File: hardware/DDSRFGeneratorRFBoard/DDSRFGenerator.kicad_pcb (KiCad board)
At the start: 2 copper layers, 72 parts, among them J1 Conn_Coaxial, K1 FINDER-44.52, K2 FINDER-44.52, K3 FINDER-44.52, Q1 Q_NPN_BEC, Q2 Q_NPN_BEC, Q3 Q_NPN_BEC, U1 TC1107-3.3VOA, U2 L7805, U3 L7805, U4 AD9832

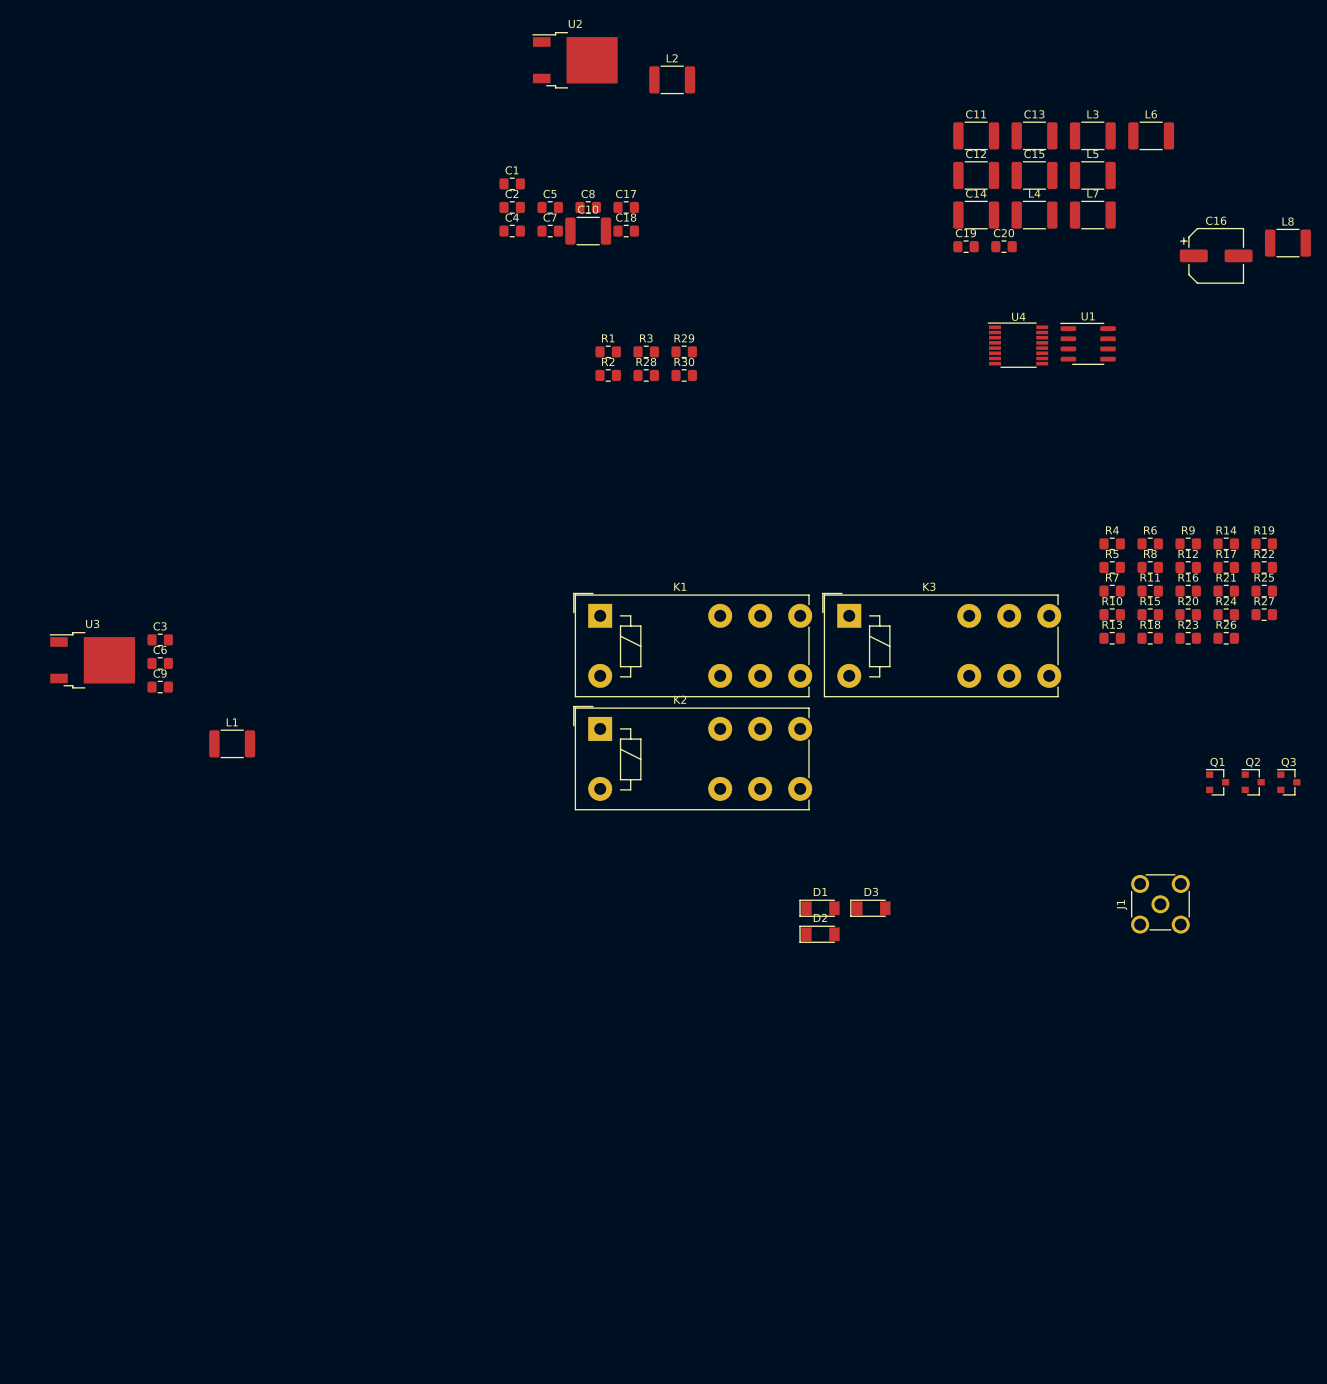
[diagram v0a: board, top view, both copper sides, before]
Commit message: draft of correct relay connections
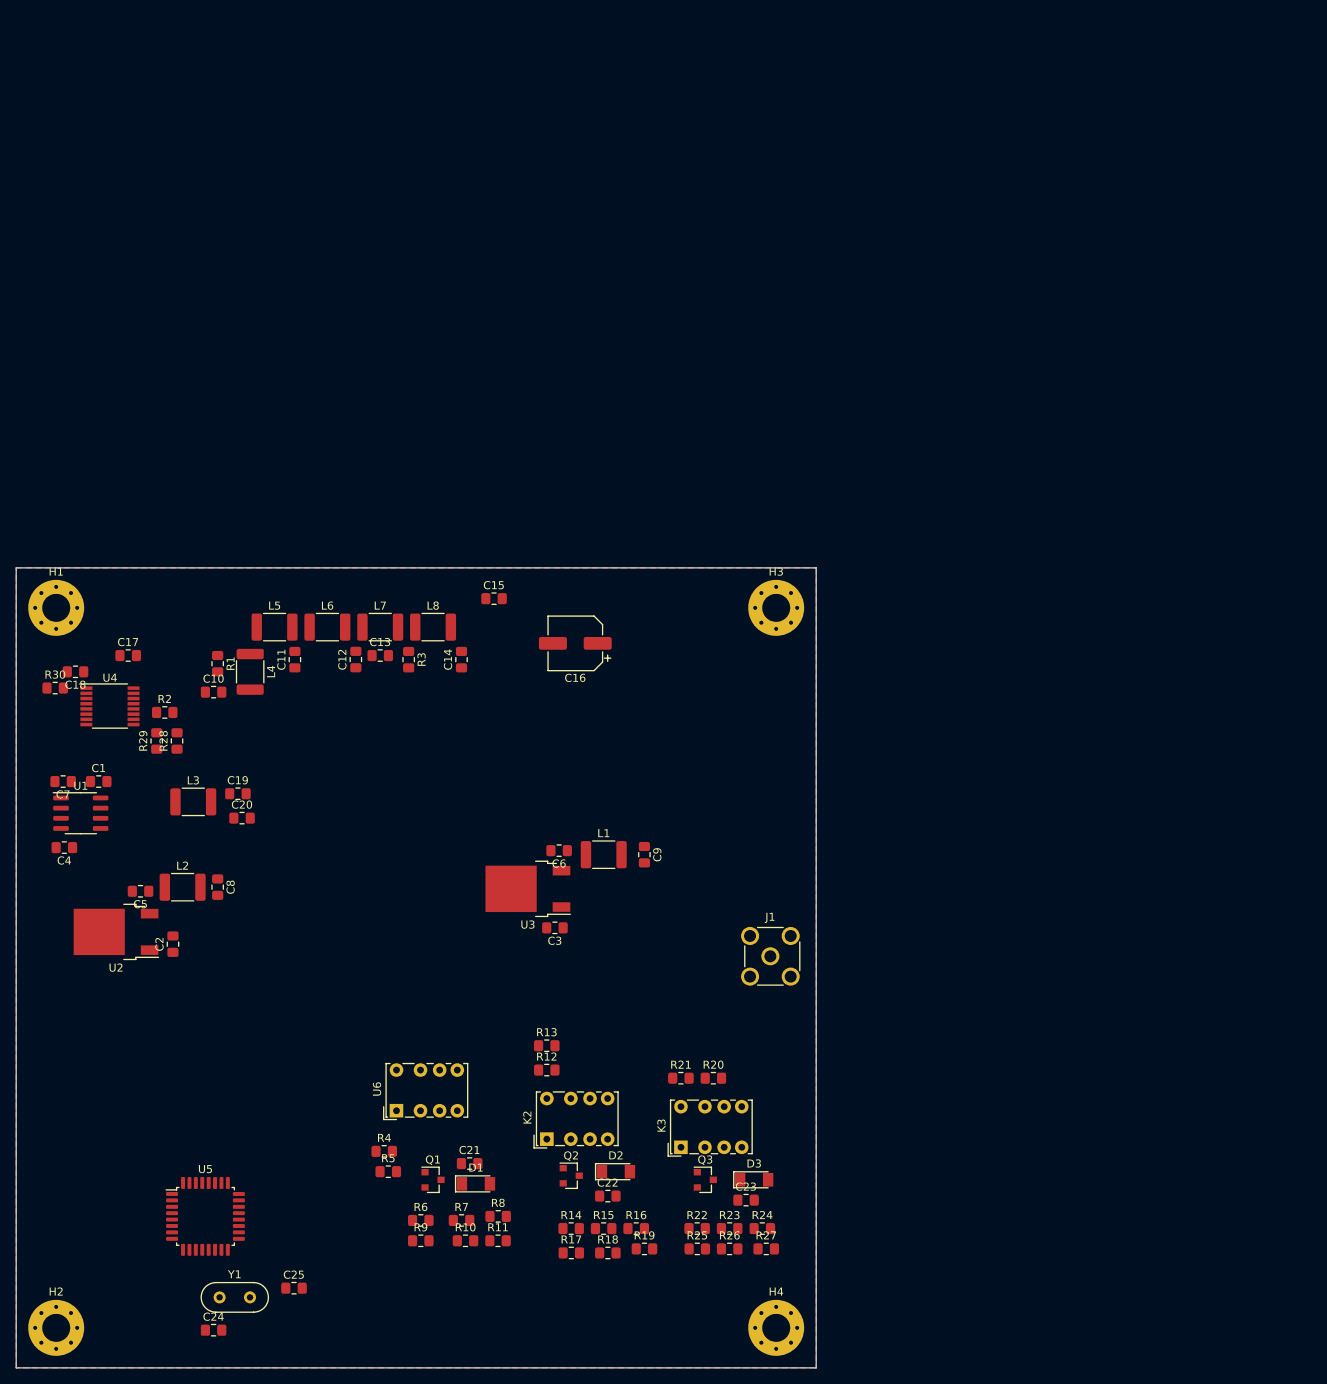
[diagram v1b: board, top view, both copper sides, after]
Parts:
- removed K1: FINDER-44.52, Relay_THT:Relay_DPDT_Finder_40.52
- added C21: 1n, Capacitor_SMD:C_0805_2012Metric_Pad1.15x1.40mm_HandSolder, F.Cu at (106.7, 124.5)
- added C22: 1n, Capacitor_SMD:C_0805_2012Metric_Pad1.15x1.40mm_HandSolder, F.Cu at (124.0, 128.5)
- added C23: 1n, Capacitor_SMD:C_0805_2012Metric_Pad1.15x1.40mm_HandSolder, F.Cu at (141.2, 129.0)
- added C24: 20p, Capacitor_SMD:C_0805_2012Metric_Pad1.15x1.40mm_HandSolder, F.Cu at (74.7, 145.3)
- added C25: 20p, Capacitor_SMD:C_0805_2012Metric_Pad1.15x1.40mm_HandSolder, F.Cu at (84.7, 140.0)
- added H1: MountingHole_Pad, MountingHole:MountingHole_3.5mm_Pad_Via, F.Cu at (55.0, 55.0)
- added H2: MountingHole_Pad, MountingHole:MountingHole_3.5mm_Pad_Via, F.Cu at (55.0, 145.0)
- added H3: MountingHole_Pad, MountingHole:MountingHole_3.5mm_Pad_Via, F.Cu at (145.0, 55.0)
- added H4: MountingHole_Pad, MountingHole:MountingHole_3.5mm_Pad_Via, F.Cu at (145.0, 145.0)
- added U5: STM32F030K6Tx, Package_QFP:LQFP-32_7x7mm_P0.8mm, F.Cu at (73.7, 131.1)
- added U6: RSM850B-6112-85-1005, Relay_THT:Relay_DPDT_Omron_G6K-2P-Y, F.Cu at (97.5, 117.9)
- added Y1: Crystal, Crystal:Crystal_HC52-6mm_Vertical, F.Cu at (75.4, 141.2)
- C10, C11, C12, C13, C14, C15: footprint Inductor_SMD:L_1812_4532Metric_Pad1.30x3.40mm_HandSolder -> Capacitor_SMD:C_0805_2012Metric_Pad1.15x1.40mm_HandSolder
- K2, K3: footprint Relay_THT:Relay_DPDT_Finder_40.52 -> Relay_THT:Relay_DPDT_Omron_G6K-2P-Y
- moved L3 139.9 mm to (72.1, 79.2)
- moved U1 138.9 mm to (58.1, 80.7)
- moved R9 129.6 mm to (100.6, 134.1)
- moved R6 124.4 mm to (100.6, 131.6)
- moved U2 123.2 mm to (62.5, 95.5), turned to 180 degrees
- moved U4 122.2 mm to (61.7, 67.3)
- moved L6 119.9 mm to (88.9, 57.4)
- moved C20 119.1 mm to (78.2, 81.3)
- moved R4 118.5 mm to (96.0, 122.9)
- moved R17 118.5 mm to (119.4, 135.6)
- moved R14 118.4 mm to (119.4, 132.6)
- moved L2 118.0 mm to (70.8, 89.9)
- moved R5 117.9 mm to (96.5, 125.5)
- moved R19 117.3 mm to (128.5, 135.1)
- moved L8 117.1 mm to (102.1, 57.4)
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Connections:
- net Net-(R29-Pad2) renamed FSELECT
- J1 pad 1: Net-(J1-Pad1) -> (no net)
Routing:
- added copper zone on F.Cu, net GND
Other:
- board outline added: 100 x 100 mm

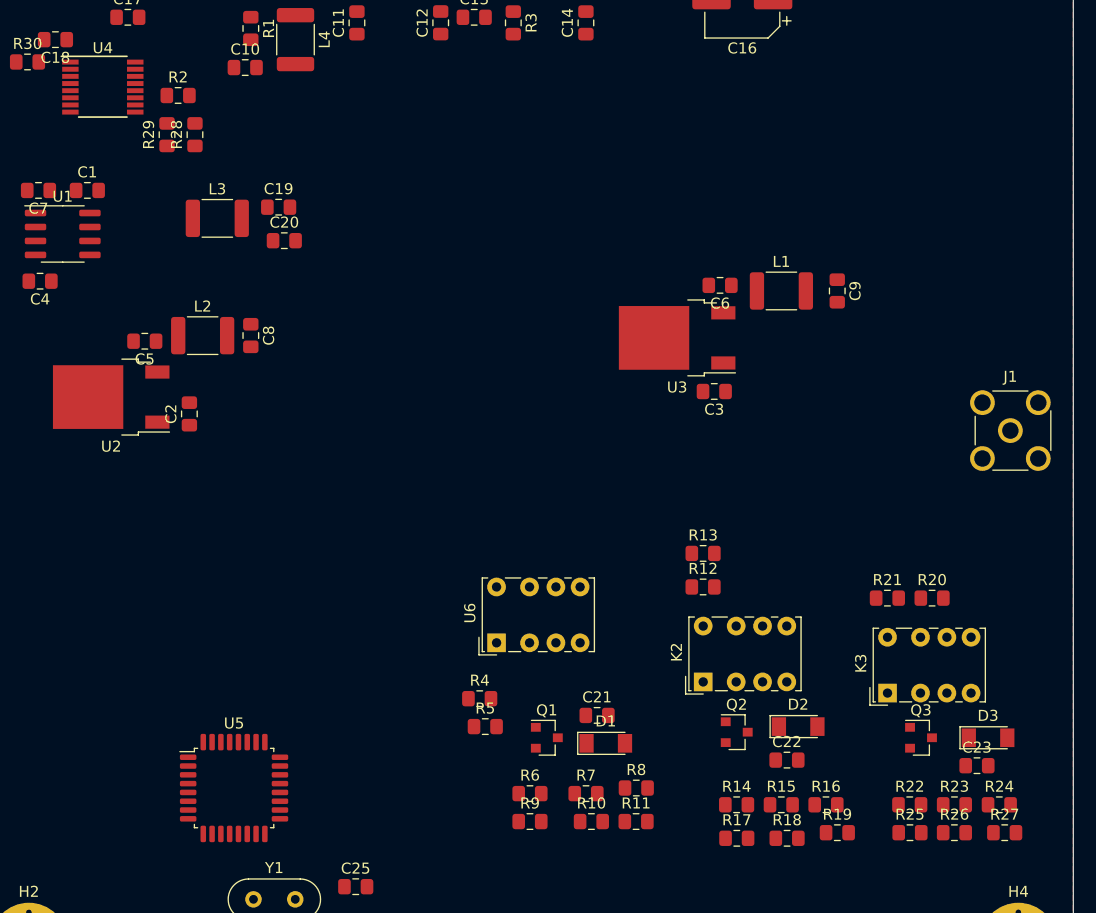
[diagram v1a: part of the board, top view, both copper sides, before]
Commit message: rougly placed submodules on pcb
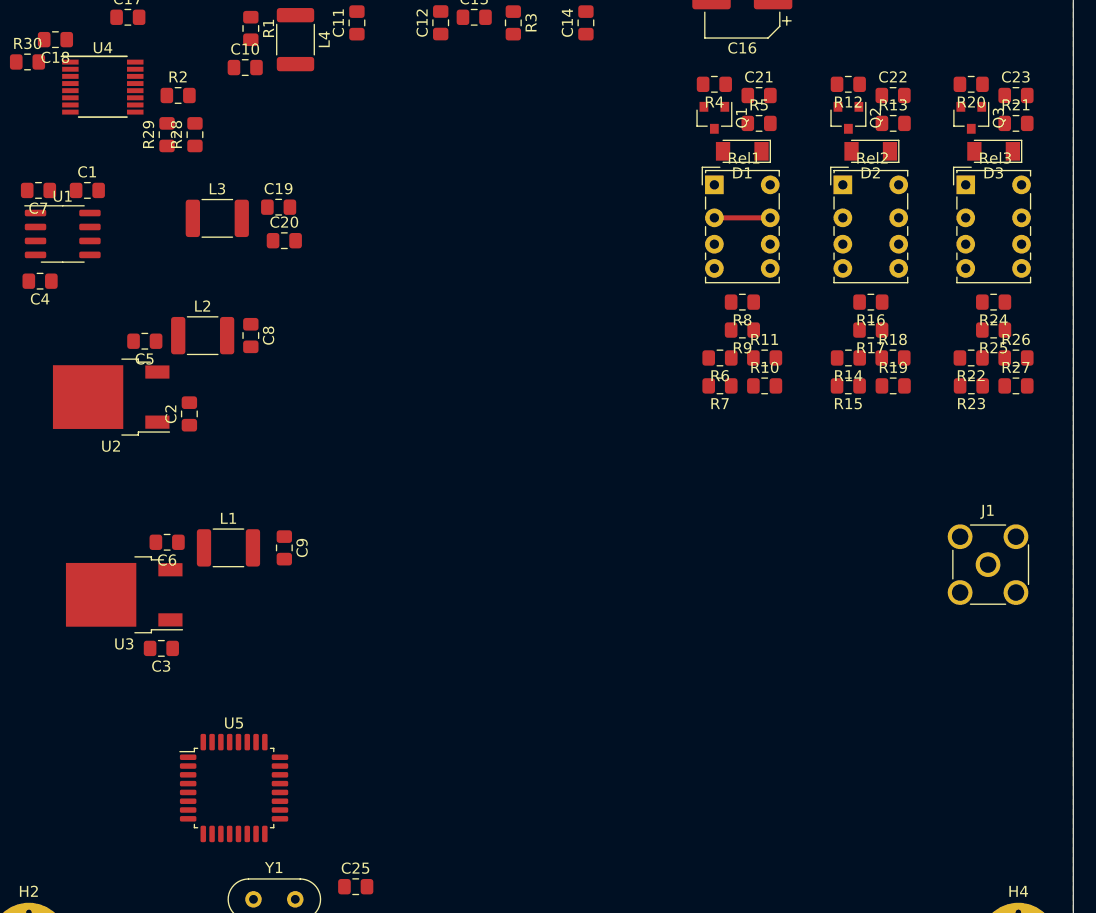
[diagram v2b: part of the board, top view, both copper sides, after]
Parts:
- removed K2, K3: FINDER-44.52, Relay_THT:Relay_DPDT_Omron_G6K-2P-Y
- removed U6: RSM850B-6112-85-1005, Relay_THT:Relay_DPDT_Omron_G6K-2P-Y
- added Rel1: RSM850B-6112-85-1005, Relay_THT:Relay_DPDT_Omron_G6K-2P-Y, F.Cu at (117.3, 76.2)
- added Rel2: RSM850B-6112-85-1005, Relay_THT:Relay_DPDT_Omron_G6K-2P-Y, F.Cu at (129.0, 76.2)
- added Rel3: RSM850B-6112-85-1005, Relay_THT:Relay_DPDT_Omron_G6K-2P-Y, F.Cu at (140.2, 76.2)
- moved C22 61.2 mm to (133.6, 68.1)
- moved C23 61.1 mm to (144.8, 68.1)
- moved R5 60.3 mm to (121.4, 70.6)
- moved R4 59.8 mm to (117.3, 67.1), turned to 180 degrees
- moved Q1 58.4 mm to (117.3, 70.1), turned to 270 degrees
- moved C21 58.3 mm to (121.4, 68.1)
- moved Q2 56.8 mm to (129.5, 70.1), turned to 270 degrees
- moved Q3 56.6 mm to (140.7, 70.1), turned to 270 degrees
- moved C3 55.5 mm to (67.0, 118.4)
- moved C6 55.5 mm to (67.6, 108.7)
- moved C9 55.5 mm to (78.2, 109.2)
- moved L1 55.5 mm to (73.2, 109.2)
- moved U3 55.5 mm to (63.7, 113.5)
- moved D1 55.3 mm to (119.9, 73.2), turned to 180 degrees
- moved D3 53.3 mm to (142.7, 73.2), turned to 180 degrees
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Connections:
- J1 pad 1: (no net) -> Net-(J1-Pad1)
- Q3 pad 3: Net-(D3-Pad2) -> (no net)
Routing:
- net Net-(Rel1-Pad2): track 0.00 -> 5.08 mm
